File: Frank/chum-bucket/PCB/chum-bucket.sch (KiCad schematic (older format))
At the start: 15 parts, among them J1 UMBILLICAL_PWR, J3 LV_PWR, J7 ESC_PWR, J8 ESC_GND

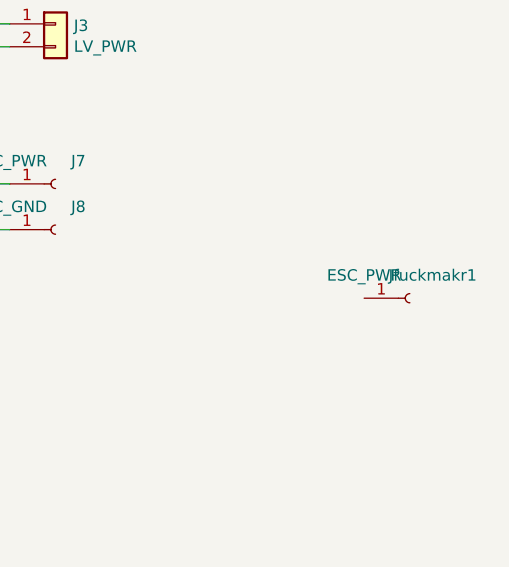
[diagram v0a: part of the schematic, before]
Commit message: lowered kicad version. Also tided up routing DRC cleared.
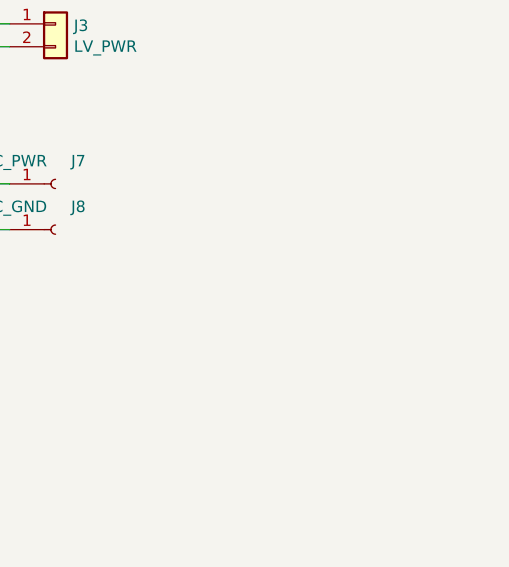
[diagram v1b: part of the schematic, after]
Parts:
- removed Jfuckmakr1: ESC_PWR, CHUM_BUCKET_FOOTPRINTS:keystone_7800, symbol Connector:Conn_01x01_Female
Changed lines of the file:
@@
-$EndComp
-$Comp
-L Connector:Conn_01x01_Female Jfuckmakr1
-U 1 1 5F1FCF5A
-P 12200 3650
-F 0 "Jfuckmakr1" H 12300 3550 50  0000 C CNN
-F 1 "ESC_PWR" H 12000 3550 50  0000 C CNN
-F 2 "CHUM_BUCKET_FOOTPRINTS:keystone_7800" H 12200 3650 50  0001 C CNN
-F 3 "http://www.keyelco.com/product-pdf.cfm?p=1118" H 12200 3650 50  0001 C CNN
-F 4 "36-7800-ND" H 12200 3650 50  0001 C CNN "Digikey"
-	1    12200 3650
-	1    0    0    1
 $EndComp
 $Comp

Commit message: routing V2
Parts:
- J1, J3: Digikey (none) -> WM1865-ND
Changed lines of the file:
@@
 F 2 "Connector_Molex:Molex_Micro-Fit_3.0_43650-0200_1x02_P3.00mm_Horizontal" H 900 2650 50  0001 C CNN
 F 3 "~" H 900 2650 50  0001 C CNN
+F 4 "WM1865-ND" H 900 2650 50  0001 C CNN "Digikey"
 	1    900  2650
 	-1   0    0    1
@@
 F 2 "Connector_Molex:Molex_Micro-Fit_3.0_43650-0200_1x02_P3.00mm_Horizontal" H 10650 2450 50  0001 C CNN
 F 3 "~" H 10650 2450 50  0001 C CNN
+F 4 "WM1865-ND" H 10650 2450 50  0001 C CNN "Digikey"
 	1    10650 2450
 	1    0    0    -1
@@
 Wire Wire Line
 	7200 3350 7200 4550
+$Comp
+L Graphic:Logo_Open_Hardware_Small #LOGO3
+U 1 1 5FB474CC
+P 12850 2300
+F 0 "#LOGO3" H 12850 2575 50  0001 C CNN
+F 1 "Logo_Open_Hardware_Small" H 12850 2075 50  0001 C CNN
+F 2 "" H 12850 2300 50  0001 C CNN
+F 3 "~" H 12850 2300 50  0001 C CNN
+F 4 "WM1845-ND" H 12850 2686 50  0000 C CNN "Digikey"
+F 5 "Digi P/N for Molex Mate" H 12850 2595 50  0000 C CNN "Note"
+	1    12850 2300
+	1    0    0    -1
+$EndComp
+$Comp
+L Graphic:Logo_Open_Hardware_Small #LOGO4
+U 1 1 5FB489B7
+P 12850 3000
+F 0 "#LOGO4" H 12850 3275 50  0001 C CNN
+F 1 "Logo_Open_Hardware_Small" H 12850 2775 50  0001 C CNN
+F 2 "" H 12850 3000 50  0001 C CNN
+F 3 "~" H 12850 3000 50  0001 C CNN
+F 4 "0430300001-12-B0-ND" H 12850 3386 50  0000 C CNN "Digikey"
+F 5 "Digi P/N for Molex BLACK 20 AWG Pre-Crimped" H 12850 3295 50  0000 C CNN "Note"
+	1    12850 3000
+	1    0    0    -1
+$EndComp
+$Comp
+L Graphic:Logo_Open_Hardware_Small #LOGO5
+U 1 1 5FB4B07B
+P 12850 3650
+F 0 "#LOGO5" H 12850 3925 50  0001 C CNN
+F 1 "Logo_Open_Hardware_Small" H 12850 3425 50  0001 C CNN
+F 2 "" H 12850 3650 50  0001 C CNN
+F 3 "~" H 12850 3650 50  0001 C CNN
+F 4 "0430300001-12-R0-ND" H 12850 4036 50  0000 C CNN "Digikey"
+F 5 "Digi P/N for Molex RED 20 AWG Pre-Crimped" H 12850 3945 50  0000 C CNN "Note"
+	1    12850 3650
+	1    0    0    -1
+$EndComp
 $EndSCHEMATC

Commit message: routing v2.1.
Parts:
- H3: footprint MountingHole:MountingHole_3.2mm_M3 -> MountingHole:MountingHole_3.2mm_M3_Pad_Via
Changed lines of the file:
@@
 F4 "SYS_PWR_OUT_PROT" I R 9800 2450 50
 F5 "ESC_PWR_EN" I L 7600 3350 50
-F6 "ANALOG_I_ESCS" I L 7600 3250 50
-F7 "ANALOG_V_SYSTEM" I L 7600 3050 50
-F8 "ANALOG_V_ESCS" I L 7600 3150 50
+F6 "ANALOG_V_SYSTEM" I L 7600 3050 50
+F7 "ANALOG_V_ESCS" I L 7600 3150 50
 $EndSheet
 Wire Wire Line
@@
 F9 "CHG_PWR_UNFUSED" I L 4150 3900 50
 F10 "ESC_PWR_EN" I R 6350 4550 50
-F11 "ANALOG_I_ESCS" I R 6350 4450 50
-F12 "ANALOG_V_SYSTEM" I R 6350 4250 50
-F13 "ANALOG_V_ESCS" I R 6350 4350 50
-F14 "BQ24617_PG" I R 6350 3950 50
+F11 "ANALOG_V_SYSTEM" I R 6350 4250 50
+F12 "ANALOG_V_ESCS" I R 6350 4350 50
+F13 "BQ24617_PG" I R 6350 3950 50
 $EndSheet
 $Comp
@@
 F 0 "H3" H 9600 5299 50  0000 L CNN
 F 1 "Top_Right" H 9600 5208 50  0000 L CNN
-F 2 "MountingHole:MountingHole_3.2mm_M3" H 9500 5250 50  0001 C CNN
+F 2 "MountingHole:MountingHole_3.2mm_M3_Pad_Via" H 9500 5250 50  0001 C CNN
 F 3 "~" H 9500 5250 50  0001 C CNN
 	1    9500 5250
@@
 	7000 3150 7600 3150
 Wire Wire Line
-	7100 3250 7600 3250
-Wire Wire Line
 	7200 3350 7600 3350
 Wire Wire Line
@@
 	7000 3150 7000 4350
 Wire Wire Line
-	7100 4450 6350 4450
-Wire Wire Line
-	7100 3250 7100 4450
-Wire Wire Line
 	7200 4550 6350 4550

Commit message: post-BOM order
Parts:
- C1, C4, C5, C6: Digikey (none) -> 1276-1009-1-ND
- J7, J8: Digikey https://www.keyelco.com/userAssets/file/M65p69.pdf -> 36-7771-ND
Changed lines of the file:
@@
 F 3 "~" H 2100 2850 50  0001 C CNN
 F 4 "50V" H 2250 2700 50  0000 C CNN "Voltage"
+F 5 "1276-1009-1-ND" H 2100 2850 50  0001 C CNN "Digikey"
 	1    2100 2850
 	1    0    0    -1
@@
 F 2 "Capacitor_SMD:C_0603_1608Metric" H 9000 5550 50  0001 C CNN
 F 3 "~" H 9000 5550 50  0001 C CNN
+F 4 "1276-1009-1-ND" H 9000 5550 50  0001 C CNN "Digikey"
 	1    9000 5550
 	1    0    0    -1
@@
 F 2 "Capacitor_SMD:C_0603_1608Metric" H 9500 5550 50  0001 C CNN
 F 3 "~" H 9500 5550 50  0001 C CNN
+F 4 "1276-1009-1-ND" H 9500 5550 50  0001 C CNN "Digikey"
 	1    9500 5550
 	1    0    0    -1
@@
 F 2 "Capacitor_SMD:C_0603_1608Metric" H 10000 5550 50  0001 C CNN
 F 3 "~" H 10000 5550 50  0001 C CNN
+F 4 "1276-1009-1-ND" H 10000 5550 50  0001 C CNN "Digikey"
 	1    10000 5550
 	1    0    0    -1
@@
 F 1 "ESC_PWR" H 10450 3050 50  0000 C CNN
 F 2 "CHUM_BUCKET_FOOTPRINTS:Keystone_7771" H 10650 3150 50  0001 C CNN
-F 3 "36-7771-ND" H 10650 3150 50  0001 C CNN
-F 4 "https://www.keyelco.com/userAssets/file/M65p69.pdf" H 10650 3150 50  0001 C CNN "Digikey"
+F 3 "https://www.keyelco.com/userAssets/file/M65p69.pdf" H 10650 3150 50  0001 C CNN
+F 4 "36-7771-ND" H 10650 3150 50  0001 C CNN "Digikey"
 	1    10650 3150
 	1    0    0    1
@@
 F 1 "ESC_GND" H 10450 3250 50  0000 C CNN
 F 2 "CHUM_BUCKET_FOOTPRINTS:Keystone_7771" H 10650 3350 50  0001 C CNN
-F 3 "36-7771-ND" H 10650 3350 50  0001 C CNN
-F 4 "https://www.keyelco.com/userAssets/file/M65p69.pdf" H 10650 3350 50  0001 C CNN "Digikey"
+F 3 "https://www.keyelco.com/userAssets/file/M65p69.pdf" H 10650 3350 50  0001 C CNN
+F 4 "36-7771-ND" H 10650 3350 50  0001 C CNN "Digikey"
 	1    10650 3350
 	1    0    0    1
@@
 	1    0    0    -1
 $EndComp
+$Comp
+L Graphic:Logo_Open_Hardware_Small #LOGO6
+U 1 1 5FE6D1B8
+P 12850 4300
+F 0 "#LOGO6" H 12850 4575 50  0001 C CNN
+F 1 "Logo_Open_Hardware_Small" H 12850 4075 50  0001 C CNN
+F 2 "" H 12850 4300 50  0001 C CNN
+F 3 "~" H 12850 4300 50  0001 C CNN
+F 4 "SMD291AX10T5-ND" H 12850 4686 50  0000 C CNN "Digikey"
+F 5 "Digi P/N for Type 5 Solder Paste" H 12850 4595 50  0000 C CNN "Note"
+	1    12850 4300
+	1    0    0    -1
+$EndComp
+$Comp
+L Graphic:Logo_Open_Hardware_Small #LOGO7
+U 1 1 5FE6D8A0
+P 12850 4950
+F 0 "#LOGO7" H 12850 5225 50  0001 C CNN
+F 1 "Logo_Open_Hardware_Small" H 12850 4725 50  0001 C CNN
+F 2 "" H 12850 4950 50  0001 C CNN
+F 3 "~" H 12850 4950 50  0001 C CNN
+F 4 "CR6A-KIT-ND" H 12850 5336 50  0000 C CNN "Digikey"
+F 5 "Digi P/N for Resistor Book" H 12850 5245 50  0000 C CNN "Note"
+	1    12850 4950
+	1    0    0    -1
+$EndComp
+$Comp
+L Graphic:Logo_Open_Hardware_Small #LOGO8
+U 1 1 5FE6DD0B
+P 12850 5600
+F 0 "#LOGO8" H 12850 5875 50  0001 C CNN
+F 1 "Logo_Open_Hardware_Small" H 12850 5375 50  0001 C CNN
+F 2 "" H 12850 5600 50  0001 C CNN
+F 3 "~" H 12850 5600 50  0001 C CNN
+F 4 "445-9005-KIT-ND" H 12850 5986 50  0000 C CNN "Digikey"
+F 5 "Digi P/N for Capacitor Book" H 12850 5895 50  0000 C CNN "Note"
+	1    12850 5600
+	1    0    0    -1
+$EndComp
